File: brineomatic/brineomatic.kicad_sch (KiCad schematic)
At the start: 9 parts, among them J1 Conn_01x04_MountingPin

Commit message: updated resistor p/ns in bom
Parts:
- R1, R2: LCSC (none) -> C25804
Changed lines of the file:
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@@
+			)
+		)
+		(property "LCSC" "C25804"
+			(at 53.34 43.18 0)
+			(effects
+				(font
+					(size 1.27 1.27)
+				)
+				(hide yes)
 			)
 		)
@@
 			(at 53.34 52.07 0)
 			(effects
+				(font
+					(size 1.27 1.27)
+				)
+				(hide yes)
+			)
+		)
+		(property "LCSC" "C25804"
+			(at 53.34 52.07 0)
+			(effects

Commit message: put 2x0 ohm between GND and USB SHIELD
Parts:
- H1, H2, H3, H4: footprint MountingHole:MountingHole_3.2mm_M3_DIN965_Pad -> yarrboard:SMTSO30XXX; LCSC (none) -> C2916369; now in the parts list
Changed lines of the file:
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@@
 		(unit 1)
 		(exclude_from_sim no)
-		(in_bom no)
+		(in_bom yes)
 		(on_board yes)
 		(dnp no)
@@
 			)
 		)
-		(property "Footprint" "MountingHole:MountingHole_3.2mm_M3_DIN965_Pad"
+		(property "Footprint" "yarrboard:SMTSO30XXX"
 			(at 105.41 166.37 0)
 			(effects
@@
 		(property "Description" ""
 			(at 105.41 166.37 0)
+			(effects
+				(font
+					(size 1.27 1.27)
+				)
+				(hide yes)
+			)
+		)
+		(property "LCSC" "C2916369"
+			(at 105.41 166.37 90)
 			(effects
 				(font
@@
 		(unit 1)
 		(exclude_from_sim no)
-		(in_bom no)
+		(in_bom yes)
 		(on_board yes)
 		(dnp no)
@@
 			)
 		)
-		(property "Footprint" "MountingHole:MountingHole_3.2mm_M3_DIN965_Pad"
+		(property "Footprint" "yarrboard:SMTSO30XXX"
 			(at 119.38 166.37 0)
 			(effects
@@
 		(property "Description" ""
 			(at 119.38 166.37 0)
+			(effects
+				(font
+					(size 1.27 1.27)
+				)
+				(hide yes)
+			)
+		)
+		(property "LCSC" "C2916369"
+			(at 119.38 166.37 90)
 			(effects
 				(font
@@
 		(unit 1)
 		(exclude_from_sim no)
-		(in_bom no)
+		(in_bom yes)
 		(on_board yes)
 		(dnp no)
@@
 			)
 		)
-		(property "Footprint" "MountingHole:MountingHole_3.2mm_M3_DIN965_Pad"
+		(property "Footprint" "yarrboard:SMTSO30XXX"
 			(at 105.41 176.53 0)
 			(effects
@@
 		(property "Description" ""
 			(at 105.41 176.53 0)
+			(effects
+				(font
+					(size 1.27 1.27)
+				)
+				(hide yes)
+			)
+		)
+		(property "LCSC" "C2916369"
+			(at 105.41 176.53 90)
 			(effects
 				(font
@@
 		(unit 1)
 		(exclude_from_sim no)
-		(in_bom no)
+		(in_bom yes)
 		(on_board yes)
 		(dnp no)
@@
 			)
 		)
-		(property "Footprint" "MountingHole:MountingHole_3.2mm_M3_DIN965_Pad"
+		(property "Footprint" "yarrboard:SMTSO30XXX"
 			(at 119.38 176.53 0)
 			(effects
@@
 			(effects
 				(font
+					(size 1.27 1.27)
+				)
+				(hide yes)
+			)
+		)
+		(property "LCSC" "C2916369"
+			(at 119.38 176.53 90)
+			(effects
+				(font

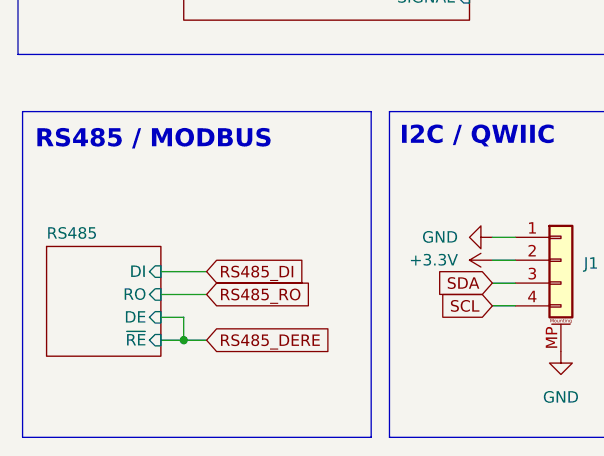
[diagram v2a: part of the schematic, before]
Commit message: updated the modbus schematic with esd and DERE combination
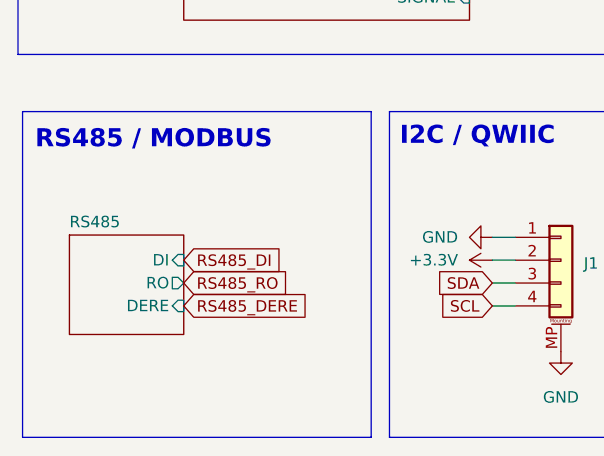
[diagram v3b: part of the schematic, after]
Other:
- sheet RS485 ports: added DERE; removed DE, ~{RE}
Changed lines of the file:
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@@
 	)
 	(junction
-		(at 41.91 176.53)
-		(diameter 0)
-		(color 0 0 0 0)
-	)
-	(junction
 		(at 96.52 92.71)
 		(diameter 0)
@@
 	(wire
 		(pts
-			(xy 39.37 173.99) (xy 41.91 173.99)
-		)
-		(stroke
-			(width 0)
-			(type default)
-		)
-	)
-	(wire
-		(pts
-			(xy 39.37 168.91) (xy 44.45 168.91)
-		)
-		(stroke
-			(width 0)
-			(type default)
-		)
-	)
-	(wire
-		(pts
 			(xy 77.47 127) (xy 73.66 127)
 		)
@@
 	(wire
 		(pts
-			(xy 39.37 171.45) (xy 44.45 171.45)
-		)
-		(stroke
-			(width 0)
-			(type default)
-		)
-	)
-	(wire
-		(pts
 			(xy 76.2 170.18) (xy 78.74 170.18)
 		)
@@
 	(wire
 		(pts
-			(xy 41.91 176.53) (xy 44.45 176.53)
-		)
-		(stroke
-			(width 0)
-			(type default)
-		)
-	)
-	(wire
-		(pts
 			(xy 77.47 123.19) (xy 77.47 127)
 		)
@@
 	(wire
 		(pts
-			(xy 41.91 173.99) (xy 41.91 176.53)
-		)
-		(stroke
-			(width 0)
-			(type default)
-		)
-	)
-	(wire
-		(pts
 			(xy 96.52 92.71) (xy 96.52 97.79)
 		)
@@
 		)
 	)
-	(wire
-		(pts
-			(xy 39.37 176.53) (xy 41.91 176.53)
-		)
-		(stroke
-			(width 0)
-			(type default)
-		)
-	)
 	(global_label "RS485_DI"
 		(shape input)
-		(at 44.45 168.91 0)
+		(at 41.91 167.64 0)
 		(fields_autoplaced yes)
 		(effects
@@
 		)
 		(property "Intersheetrefs" "${INTERSHEET_REFS}"
-			(at 56.3856 168.91 0)
+			(at 53.8456 167.64 0)
 			(effects
 				(font
@@
 	(global_label "RS485_RO"
 		(shape input)
-		(at 44.45 171.45 0)
+		(at 41.91 170.18 0)
 		(fields_autoplaced yes)
 		(effects
@@
 		)
 		(property "Intersheetrefs" "${INTERSHEET_REFS}"
-			(at 57.1113 171.45 0)
+			(at 54.5713 170.18 0)
 			(effects
 				(font
@@
 	(global_label "RS485_DERE"
 		(shape input)
-		(at 44.45 176.53 0)
+		(at 41.91 172.72 0)
 		(fields_autoplaced yes)
 		(effects
@@
 		)
 		(property "Intersheetrefs" "${INTERSHEET_REFS}"
-			(at 59.3488 176.53 0)
+			(at 56.8088 172.72 0)
 			(effects
 				(font
@@
 	)
 	(sheet
-		(at 26.67 166.116)
-		(size 12.7 12.192)
+		(at 29.21 164.846)
+		(size 12.7 11.049)
 		(exclude_from_sim no)
 		(in_bom yes)
@@
 		)
 		(property "Sheetname" "RS485"
-			(at 26.67 165.4044 0)
+			(at 29.21 164.1344 0)
 			(effects
 				(font
@@
 		)
 		(property "Sheetfile" "rs485.kicad_sch"
-			(at 26.67 178.8926 0)
+			(at 29.21 176.4796 0)
 			(effects
 				(font
@@
 			)
 		)
-		(pin "DE" input
-			(at 39.37 173.99 0)
+		(pin "DERE" input
+			(at 41.91 172.72 0)
 			(effects
 				(font
@@
 		)
 		(pin "DI" input
-			(at 39.37 168.91 0)
-			(effects
-				(font
-					(size 1.27 1.27)
-				)
-				(justify right)
-			)
-		)
-		(pin "RO" input
-			(at 39.37 171.45 0)
+			(at 41.91 167.64 0)
 			(effects
 				(font
@@
 			)
 		)
-		(pin "~{RE}" input
-			(at 39.37 176.53 0)
+		(pin "RO" output
+			(at 41.91 170.18 0)
 			(effects
 				(font

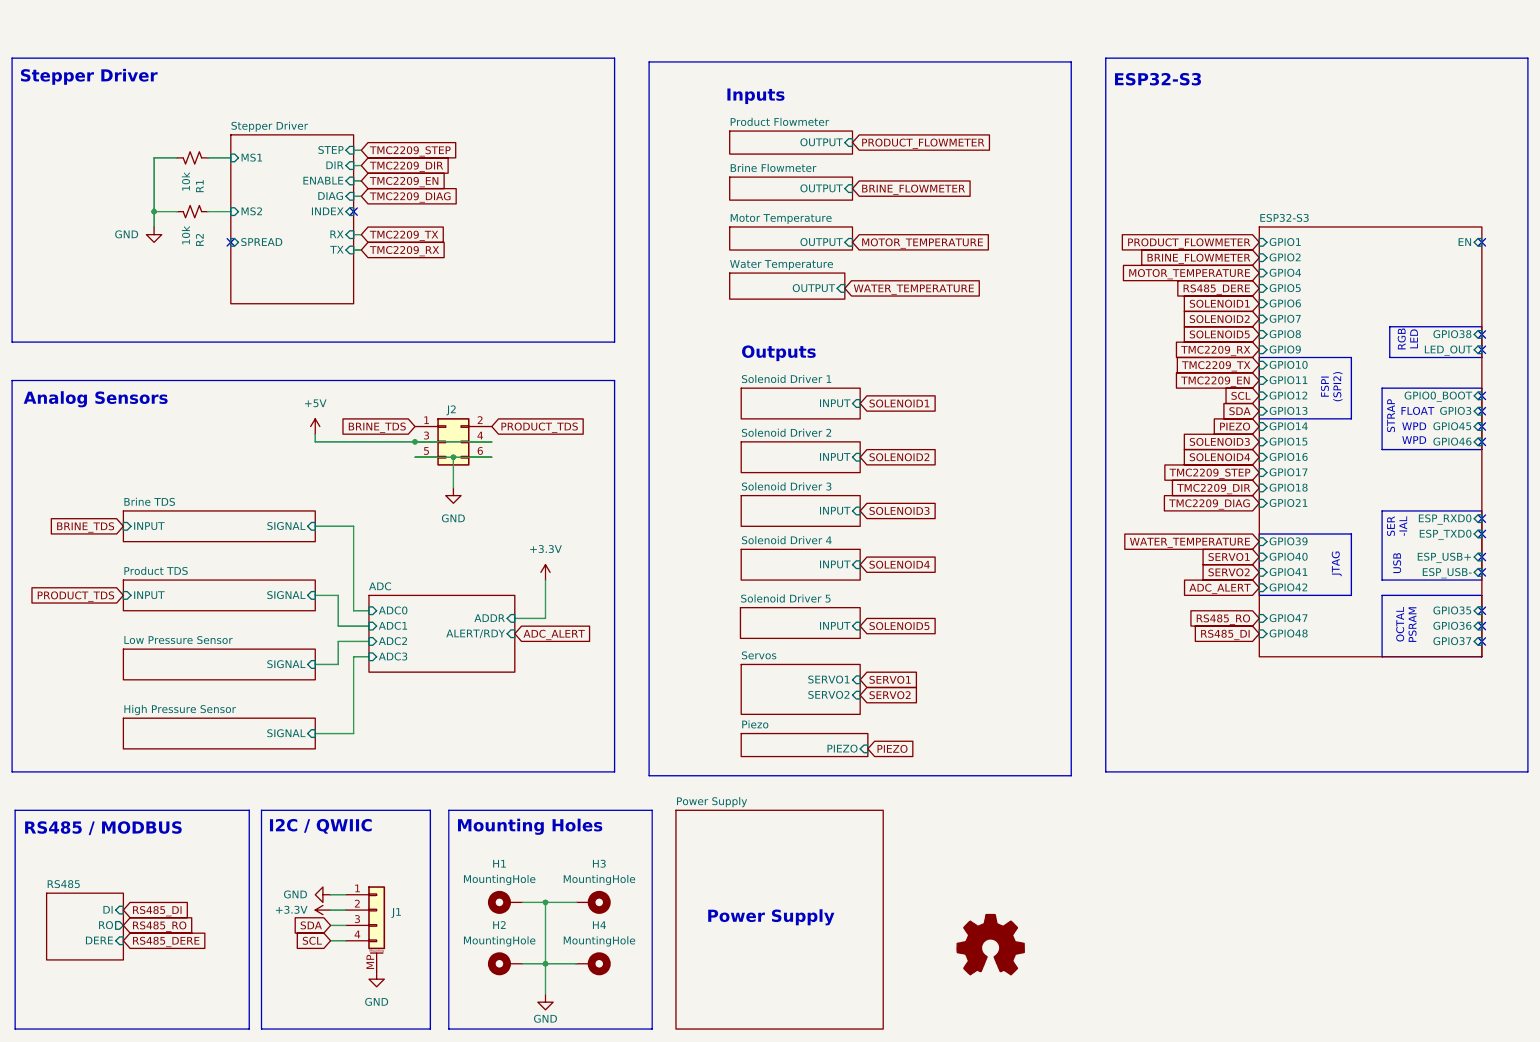
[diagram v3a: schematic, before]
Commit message: updated analog sensor esd schematic
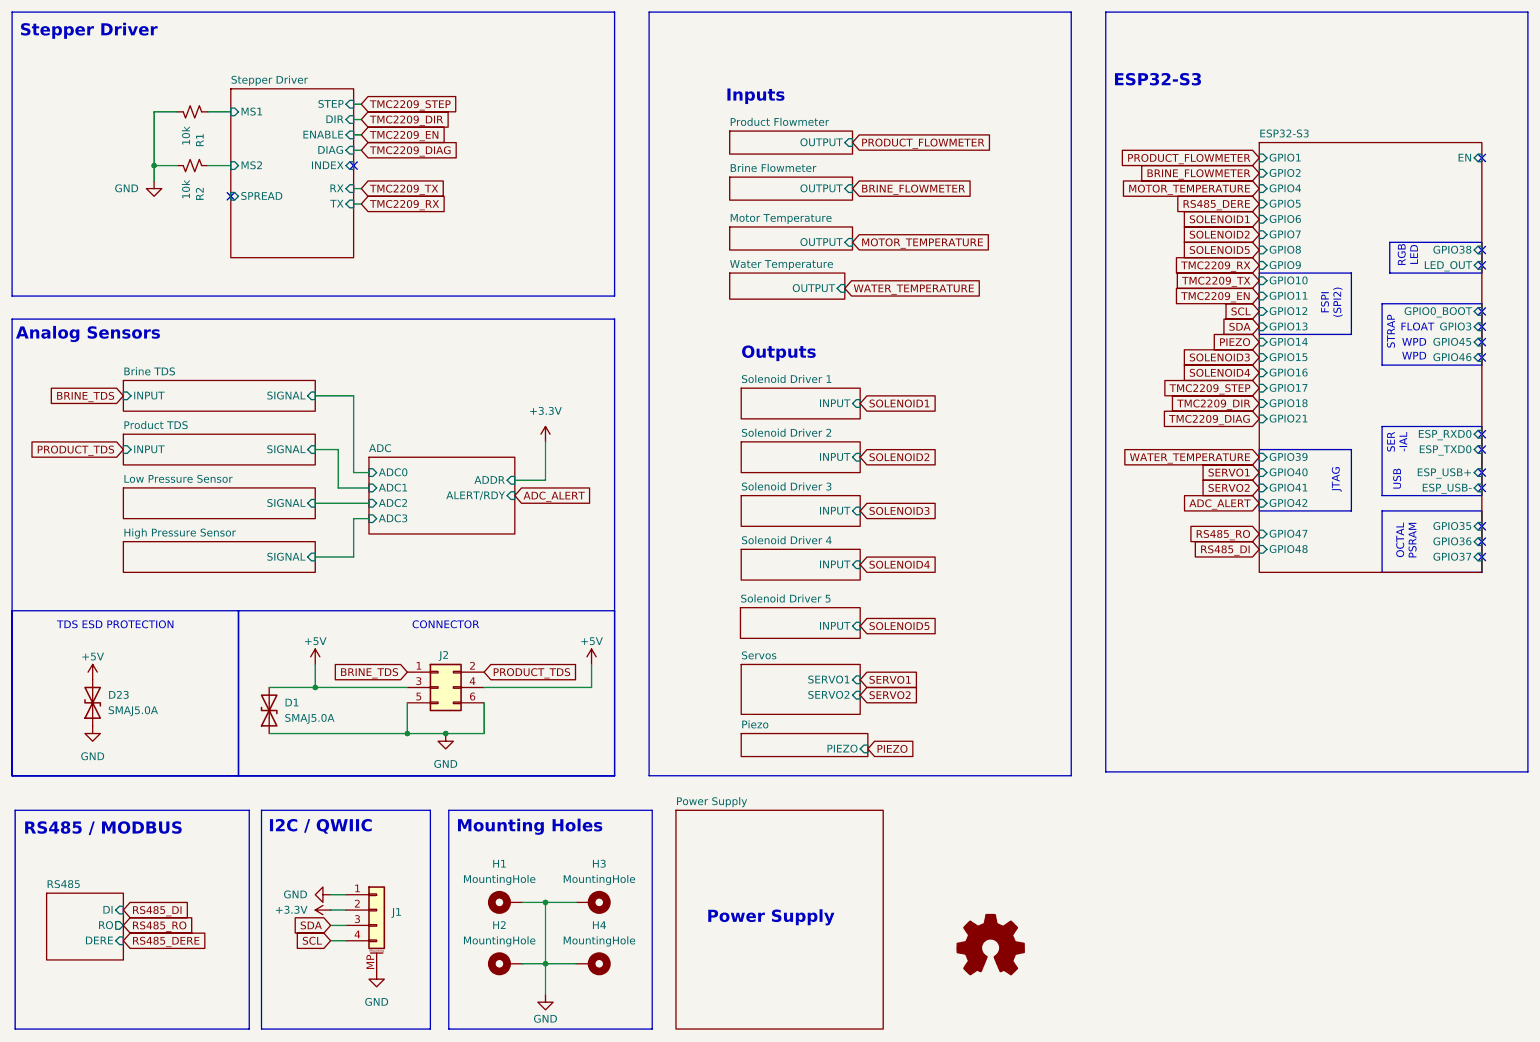
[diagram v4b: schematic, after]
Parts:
- added D1, D23: SMAJ5.0A, Diode_SMD:D_SMA, symbol Device:D_TVS
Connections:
- net +5V: now also D1.2 (A2), D23.2 (A2)
- net GND: now also D1.1 (A1), D23.1 (A1)
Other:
- note added: "CONNECTOR"
- note added: "TDS ESD PROTECTION"
- moved on the sheet: J2, R1, R2

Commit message: added bulk cap after ideal diode
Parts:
- renumbered D23 to D1, D1 to D2
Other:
- note added: "TDS CONNECTIONS"
- note removed: "CONNECTOR"
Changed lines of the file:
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@@
 		)
 	)
-	(text "CONNECTOR"
+	(text "TDS CONNECTIONS"
 		(exclude_from_sim no)
 		(at 95.25 120.65 0)
@@
 		(on_board yes)
 		(dnp no)
-		(property "Reference" "#PWR074"
+		(property "Reference" "#PWR01"
 			(at 36.83 133.35 0)
 			(effects
@@
 			(project "brineomatic"
 				(path "/96477ae2-ef08-48f3-8dd4-fe4478541f68"
-					(reference "#PWR074")
+					(reference "#PWR01")
 					(unit 1)
 				)
@@
 		(dnp no)
 		(fields_autoplaced yes)
-		(property "Reference" "#PWR04"
+		(property "Reference" "#PWR06"
 			(at 80.01 167.64 0)
 			(effects
@@
 			(project "brineomatic"
 				(path "/96477ae2-ef08-48f3-8dd4-fe4478541f68"
-					(reference "#PWR04")
+					(reference "#PWR06")
 					(unit 1)
 				)
@@
 		(on_board yes)
 		(dnp no)
-		(property "Reference" "#PWR09"
+		(property "Reference" "#PWR011"
 			(at 119.38 130.81 0)
 			(effects
@@
 			(project "brineomatic"
 				(path "/96477ae2-ef08-48f3-8dd4-fe4478541f68"
-					(reference "#PWR09")
+					(reference "#PWR011")
 					(unit 1)
 				)
@@
 		(dnp no)
 		(fields_autoplaced yes)
-		(property "Reference" "#PWR01"
+		(property "Reference" "#PWR03"
 			(at 46.99 53.34 0)
 			(effects
@@
 			(project "brineomatic"
 				(path "/96477ae2-ef08-48f3-8dd4-fe4478541f68"
-					(reference "#PWR01")
+					(reference "#PWR03")
 					(unit 1)
 				)
@@
 		(on_board yes)
 		(dnp no)
-		(property "Reference" "D1"
+		(property "Reference" "D2"
 			(at 68.58 133.35 90)
 			(effects
@@
 			(project "brineomatic"
 				(path "/96477ae2-ef08-48f3-8dd4-fe4478541f68"
-					(reference "D1")
+					(reference "D2")
 					(unit 1)
 				)
@@
 		(dnp no)
 		(fields_autoplaced yes)
-		(property "Reference" "#PWR06"
+		(property "Reference" "#PWR08"
 			(at 95.25 144.78 0)
 			(effects
@@
 			(project "brineomatic"
 				(path "/96477ae2-ef08-48f3-8dd4-fe4478541f68"
-					(reference "#PWR06")
+					(reference "#PWR08")
 					(unit 1)
 				)
@@
 		(on_board yes)
 		(dnp no)
-		(property "Reference" "#PWR08"
+		(property "Reference" "#PWR010"
 			(at 111.76 187.96 0)
 			(effects
@@
 			(project "brineomatic"
 				(path "/96477ae2-ef08-48f3-8dd4-fe4478541f68"
-					(reference "#PWR08")
+					(reference "#PWR010")
 					(unit 1)
 				)
@@
 		(dnp no)
 		(fields_autoplaced yes)
-		(property "Reference" "#PWR05"
+		(property "Reference" "#PWR07"
 			(at 83.82 184.15 0)
 			(effects
@@
 			(project "brineomatic"
 				(path "/96477ae2-ef08-48f3-8dd4-fe4478541f68"
-					(reference "#PWR05")
+					(reference "#PWR07")
 					(unit 1)
 				)
@@
 		(dnp no)
 		(fields_autoplaced yes)
-		(property "Reference" "#PWR07"
+		(property "Reference" "#PWR09"
 			(at 111.76 93.98 0)
 			(effects
@@
 			(project ""
 				(path "/96477ae2-ef08-48f3-8dd4-fe4478541f68"
-					(reference "#PWR07")
+					(reference "#PWR09")
 					(unit 1)
 				)
@@
 		(dnp no)
 		(fields_autoplaced yes)
-		(property "Reference" "#PWR03"
+		(property "Reference" "#PWR05"
 			(at 69.85 165.1 0)
 			(effects
@@
 			(project "brineomatic"
 				(path "/96477ae2-ef08-48f3-8dd4-fe4478541f68"
-					(reference "#PWR03")
+					(reference "#PWR05")
 					(unit 1)
 				)
@@
 		(dnp no)
 		(fields_autoplaced yes)
-		(property "Reference" "#PWR073"
+		(property "Reference" "#PWR02"
 			(at 36.83 143.51 0)
 			(effects
@@
 			(project "brineomatic"
 				(path "/96477ae2-ef08-48f3-8dd4-fe4478541f68"
-					(reference "#PWR073")
+					(reference "#PWR02")
 					(unit 1)
 				)
@@
 		(on_board yes)
 		(dnp no)
-		(property "Reference" "D23"
+		(property "Reference" "D1"
 			(at 39.37 132.08 90)
 			(effects
@@
 			(project "brineomatic"
 				(path "/96477ae2-ef08-48f3-8dd4-fe4478541f68"
-					(reference "D23")
+					(reference "D1")
 					(unit 1)
 				)
@@
 		(on_board yes)
 		(dnp no)
-		(property "Reference" "#PWR02"
+		(property "Reference" "#PWR04"
 			(at 73.66 130.81 0)
 			(effects
@@
 			(project ""
 				(path "/96477ae2-ef08-48f3-8dd4-fe4478541f68"
-					(reference "#PWR02")
+					(reference "#PWR04")
 					(unit 1)
 				)

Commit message: cleaned up hierarchical pin settings
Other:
- sheet Piezo renamed Buzzer
- sheet Buzzer ports: added BUZZER; removed PIEZO
- sheet Motor Temperature ports: added I/O; removed OUTPUT
- sheet Water Temperature ports: added I/O; removed OUTPUT
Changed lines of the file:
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@@
 	(wire
 		(pts
-			(xy 80.01 48.26) (xy 81.28 48.26)
-		)
-		(stroke
-			(width 0)
-			(type default)
-		)
-	)
-	(wire
-		(pts
 			(xy 88.9 138.43) (xy 95.25 138.43)
 		)
@@
 	(wire
 		(pts
-			(xy 81.28 39.37) (xy 80.01 39.37)
-		)
-		(stroke
-			(width 0)
-			(type default)
-		)
-	)
-	(wire
-		(pts
 			(xy 59.69 35.56) (xy 55.88 35.56)
 		)
@@
 	(wire
 		(pts
-			(xy 81.28 50.8) (xy 80.01 50.8)
-		)
-		(stroke
-			(width 0)
-			(type default)
-		)
-	)
-	(wire
-		(pts
 			(xy 111.76 96.52) (xy 111.76 90.17)
 		)
@@
 	(wire
 		(pts
-			(xy 81.28 41.91) (xy 80.01 41.91)
-		)
-		(stroke
-			(width 0)
-			(type default)
-		)
-	)
-	(wire
-		(pts
 			(xy 46.99 46.99) (xy 46.99 44.45)
 		)
@@
 	(wire
 		(pts
-			(xy 81.28 36.83) (xy 80.01 36.83)
-		)
-		(stroke
-			(width 0)
-			(type default)
-		)
-	)
-	(wire
-		(pts
 			(xy 77.47 91.44) (xy 73.66 91.44)
 		)
@@
 	(wire
 		(pts
-			(xy 81.28 34.29) (xy 80.01 34.29)
-		)
-		(stroke
-			(width 0)
-			(type default)
-		)
-	)
-	(wire
-		(pts
 			(xy 46.99 35.56) (xy 46.99 44.45)
 		)
@@
 	(global_label "WATER_TEMPERATURE"
 		(shape input)
-		(at 161.29 64.77 0)
+		(at 162.56 64.77 0)
 		(fields_autoplaced yes)
 		(effects
@@
 		)
 		(property "Intersheetrefs" "${INTERSHEET_REFS}"
-			(at 184.2321 64.77 0)
+			(at 185.5021 64.77 0)
 			(effects
 				(font
@@
 	(global_label "TMC2209_DIAG"
 		(shape input)
-		(at 81.28 41.91 0)
+		(at 80.01 41.91 0)
 		(fields_autoplaced yes)
 		(effects
@@
 		)
 		(property "Intersheetrefs" "${INTERSHEET_REFS}"
-			(at 97.9932 41.91 0)
+			(at 96.7232 41.91 0)
 			(effects
 				(font
@@
 	(global_label "TMC2209_RX"
 		(shape input)
-		(at 81.28 50.8 0)
+		(at 80.01 50.8 0)
 		(fields_autoplaced yes)
 		(effects
@@
 		)
 		(property "Intersheetrefs" "${INTERSHEET_REFS}"
-			(at 96.2393 50.8 0)
+			(at 94.9693 50.8 0)
 			(effects
 				(font
@@
 	(global_label "TMC2209_EN"
 		(shape input)
-		(at 81.28 39.37 0)
+		(at 80.01 39.37 0)
 		(fields_autoplaced yes)
 		(effects
@@
 		)
 		(property "Intersheetrefs" "${INTERSHEET_REFS}"
-			(at 96.2393 39.37 0)
+			(at 94.9693 39.37 0)
 			(effects
 				(font
@@
 		)
 	)
-	(global_label "PIEZO"
+	(global_label "BUZZER"
 		(shape input)
 		(at 165.1 140.97 0)
@@
 		)
 		(property "Intersheetrefs" "${INTERSHEET_REFS}"
-			(at 173.649 140.97 0)
+			(at 175.5237 140.97 0)
 			(effects
 				(font
@@
 		)
 	)
-	(global_label "PIEZO"
+	(global_label "BUZZER"
 		(shape input)
 		(at 229.87 73.66 180)
@@
 		)
 		(property "Intersheetrefs" "${INTERSHEET_REFS}"
-			(at 221.321 73.66 0)
+			(at 219.4463 73.66 0)
 			(effects
 				(font
@@
 	(global_label "TMC2209_DIR"
 		(shape input)
-		(at 81.28 36.83 0)
+		(at 80.01 36.83 0)
 		(fields_autoplaced yes)
 		(effects
@@
 		)
 		(property "Intersheetrefs" "${INTERSHEET_REFS}"
-			(at 96.9046 36.83 0)
+			(at 95.6346 36.83 0)
 			(effects
 				(font
@@
 	(global_label "TMC2209_STEP"
 		(shape input)
-		(at 81.28 34.29 0)
+		(at 80.01 34.29 0)
 		(fields_autoplaced yes)
 		(effects
@@
 		)
 		(property "Intersheetrefs" "${INTERSHEET_REFS}"
-			(at 98.3559 34.29 0)
+			(at 97.0859 34.29 0)
 			(effects
 				(font
@@
 	(global_label "TMC2209_TX"
 		(shape input)
-		(at 81.28 48.26 0)
+		(at 80.01 48.26 0)
 		(fields_autoplaced yes)
 		(effects
@@
 		)
 		(property "Intersheetrefs" "${INTERSHEET_REFS}"
-			(at 95.9369 48.26 0)
+			(at 94.6669 48.26 0)
 			(effects
 				(font
@@
 			)
 		)
-		(pin "TX" input
+		(pin "TX" output
 			(at 80.01 50.8 0)
 			(effects
@@
 			)
 		)
-		(pin "DIAG" input
+		(pin "DIAG" output
 			(at 80.01 41.91 0)
 			(effects
@@
 			)
 		)
-		(pin "INDEX" input
+		(pin "INDEX" output
 			(at 80.01 44.45 0)
 			(effects
@@
 	(sheet
 		(at 142.24 62.23)
-		(size 19.05 4.318)
+		(size 20.32 4.318)
 		(exclude_from_sim no)
 		(in_bom yes)
@@
 			)
 		)
-		(pin "OUTPUT" input
-			(at 161.29 64.77 0)
+		(pin "I{slash}O" bidirectional
+			(at 162.56 64.77 0)
 			(effects
 				(font
@@
 			)
 		)
-		(pin "SIGNAL" input
+		(pin "SIGNAL" output
 			(at 73.66 91.44 0)
 			(effects
@@
 			)
 		)
-		(pin "OUTPUT" input
+		(pin "I{slash}O" bidirectional
 			(at 162.56 57.15 0)
 			(effects
@@
 			)
 		)
-		(pin "OUTPUT" input
+		(pin "OUTPUT" output
 			(at 162.56 40.64 0)
 			(effects
@@
 			)
 		)
-		(pin "SIGNAL" input
+		(pin "SIGNAL" output
 			(at 73.66 82.55 0)
 			(effects
@@
 			)
 		)
-		(pin "OUTPUT" input
+		(pin "OUTPUT" output
 			(at 162.56 48.26 0)
 			(effects
@@
 			)
 		)
-		(pin "SIGNAL" input
+		(pin "SIGNAL" output
 			(at 73.66 100.33 0)
 			(effects
@@
 			(color 0 0 0 0.0000)
 		)
-		(property "Sheetname" "Piezo"
+		(property "Sheetname" "Buzzer"
 			(at 144.145 137.7184 0)
 			(effects
@@
 			)
 		)
-		(pin "PIEZO" input
+		(pin "BUZZER" input
 			(at 165.1 140.97 0)
 			(effects
@@
 			)
 		)
-		(pin "SIGNAL" input
+		(pin "SIGNAL" output
 			(at 73.66 109.22 0)
 			(effects
